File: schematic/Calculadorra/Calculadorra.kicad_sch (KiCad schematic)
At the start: 24 parts, among them U1 ATmega328-P, U2 LCD-016N002L

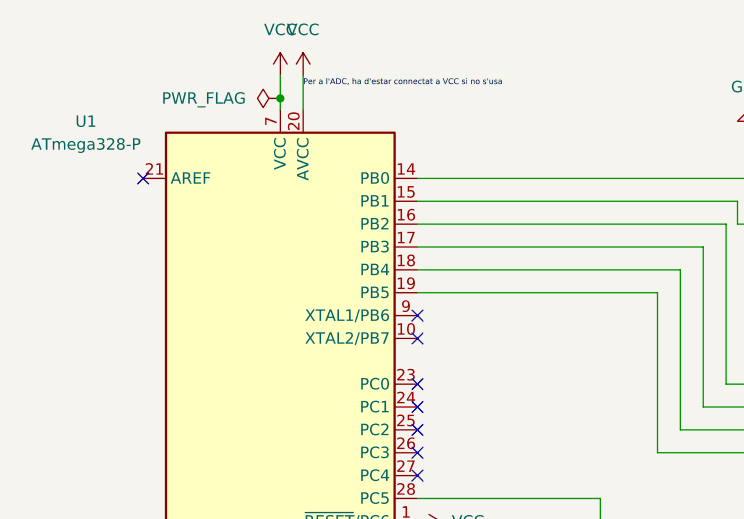
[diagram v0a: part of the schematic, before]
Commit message: Fix scan matrix for 5x4
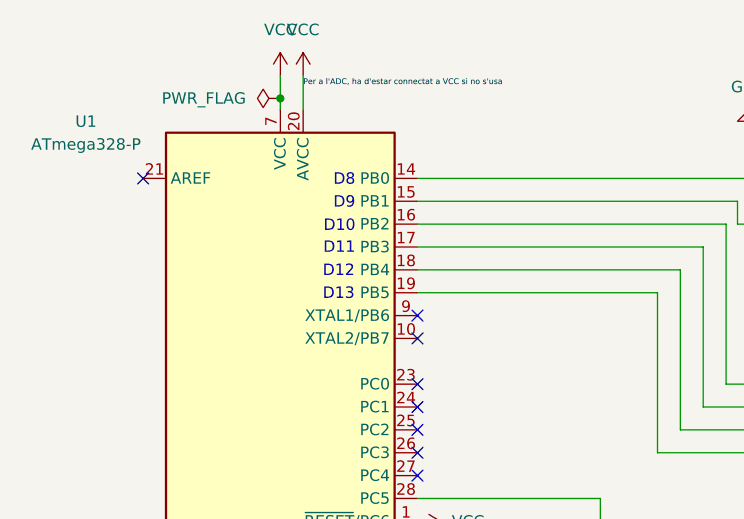
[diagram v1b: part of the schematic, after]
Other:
- note added: "D10"
- note added: "D11"
- note added: "D12"
- note added: "D13"
- note added: "D8"
- note added: "D9"
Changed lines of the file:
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@@
+		)
+	)
+	(text "D11"
+		(exclude_from_sim no)
+		(at 71.3163 58.6163 0)
+		(effects
+			(font
+				(size 1.27 1.27)
+			)
+		)
+	)
+	(text "D13"
+		(exclude_from_sim no)
+		(at 71.2559 63.7354 0)
+		(effects
+			(font
+				(size 1.27 1.27)
+			)
+		)
+	)
+	(text "D9"
+		(exclude_from_sim no)
+		(at 71.882 53.594 0)
+		(effects
+			(font
+				(size 1.27 1.27)
+			)
+		)
+	)
+	(text "D12"
+		(exclude_from_sim no)
+		(at 71.2596 61.1947 0)
+		(effects
+			(font
+				(size 1.27 1.27)
+			)
+		)
+	)
+	(text "D8"
+		(exclude_from_sim no)
+		(at 71.882 51.054 0)
+		(effects
+			(font
+				(size 1.27 1.27)
+			)
+		)
+	)
+	(text "D10"
+		(exclude_from_sim no)
+		(at 71.3446 56.1795 0)
+		(effects
+			(font
+				(size 1.27 1.27)
+			)
 		)
 	)

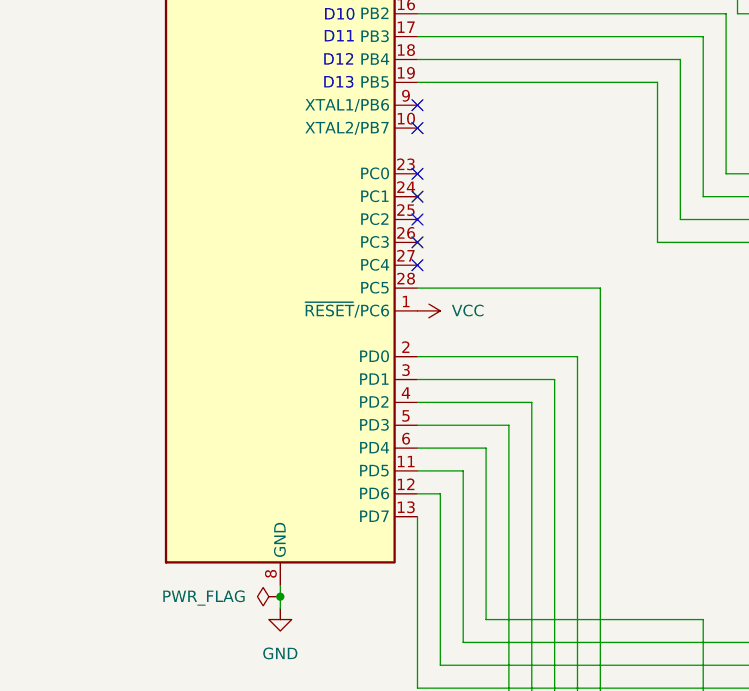
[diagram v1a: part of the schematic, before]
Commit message: Add arduino uno schematics to mega320p
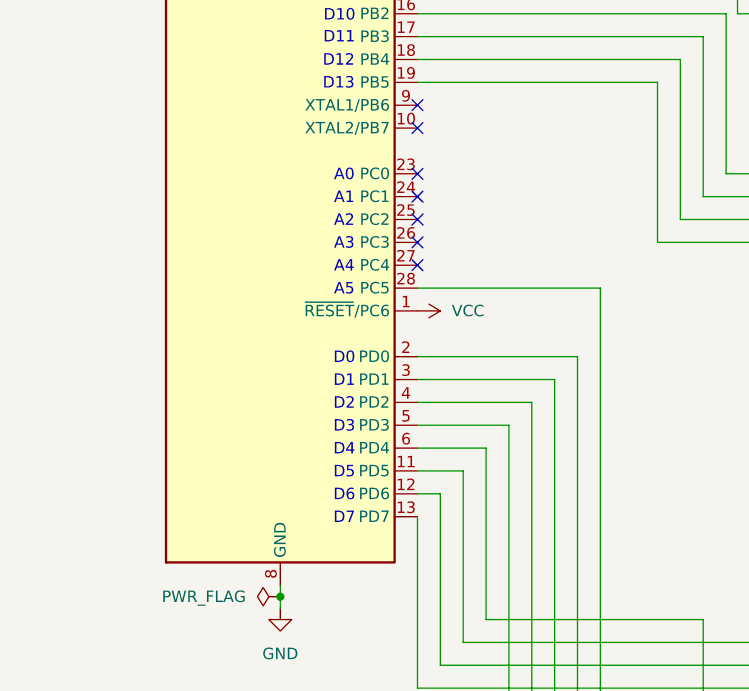
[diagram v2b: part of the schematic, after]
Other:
- note added: "A0"
- note added: "A1"
- note added: "A2"
- note added: "A3"
- note added: "A4"
- note added: "A5"
- note added: "D0"
- note added: "D1"
- note added: "D2"
- note added: "D3"
- note added: "D4"
- note added: "D5"
- note added: "D6"
- note added: "D7"
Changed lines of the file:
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@@
+		)
+	)
+	(text "D4"
+		(exclude_from_sim no)
+		(at 71.882 104.394 0)
+		(effects
+			(font
+				(size 1.27 1.27)
+			)
 		)
 	)
@@
 		)
 	)
+	(text "D3"
+		(exclude_from_sim no)
+		(at 71.882 101.854 0)
+		(effects
+			(font
+				(size 1.27 1.27)
+			)
+		)
+	)
 	(text "D12"
 		(exclude_from_sim no)
 		(at 71.2596 61.1947 0)
+		(effects
+			(font
+				(size 1.27 1.27)
+			)
+		)
+	)
+	(text "D1"
+		(exclude_from_sim no)
+		(at 71.882 96.774 0)
+		(effects
+			(font
+				(size 1.27 1.27)
+			)
+		)
+	)
+	(text "A1"
+		(exclude_from_sim no)
+		(at 71.882 76.454 0)
+		(effects
+			(font
+				(size 1.27 1.27)
+			)
+		)
+	)
+	(text "D0"
+		(exclude_from_sim no)
+		(at 71.882 94.234 0)
+		(effects
+			(font
+				(size 1.27 1.27)
+			)
+		)
+	)
+	(text "D7"
+		(exclude_from_sim no)
+		(at 71.882 112.014 0)
 		(effects
 			(font
@@
 		)
 	)
+	(text "A0\n"
+		(exclude_from_sim no)
+		(at 71.882 73.914 0)
+		(effects
+			(font
+				(size 1.27 1.27)
+			)
+		)
+	)
+	(text "A3"
+		(exclude_from_sim no)
+		(at 71.882 81.534 0)
+		(effects
+			(font
+				(size 1.27 1.27)
+			)
+		)
+	)
+	(text "A4"
+		(exclude_from_sim no)
+		(at 71.882 84.074 0)
+		(effects
+			(font
+				(size 1.27 1.27)
+			)
+		)
+	)
+	(text "D6"
+		(exclude_from_sim no)
+		(at 71.882 109.474 0)
+		(effects
+			(font
+				(size 1.27 1.27)
+			)
+		)
+	)
 	(text "D10"
 		(exclude_from_sim no)
@@
 		(effects
 			(font
+				(size 1.27 1.27)
+			)
+		)
+	)
+	(text "D5"
+		(exclude_from_sim no)
+		(at 71.882 106.934 0)
+		(effects
+			(font
+				(size 1.27 1.27)
+			)
+		)
+	)
+	(text "A5"
+		(exclude_from_sim no)
+		(at 71.882 86.614 0)
+		(effects
+			(font
+				(size 1.27 1.27)
+			)
+		)
+	)
+	(text "D2"
+		(exclude_from_sim no)
+		(at 71.882 99.314 0)
+		(effects
+			(font
+				(size 1.27 1.27)
+			)
+		)
+	)
+	(text "A2"
+		(exclude_from_sim no)
+		(at 71.882 78.994 0)
+		(effects
+			(font

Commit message: No idea what changed
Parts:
- renumbered B_( to B_(1, B_) to B_)1, B_= to B_=1, B_Add to B_Add1, B_Left to B_Left1, B_Mul to B_Mul1, B_On to B_On1, B_Right to B_Right1, B_Shift to B_Shift1, B_Sub to B_Sub1
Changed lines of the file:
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@@
 		(on_board yes)
 		(dnp no)
-		(property "Reference" "B_Left"
+		(property "Reference" "B_Left1"
 			(at 119.38 132.334 0)
 			(effects
@@
 			(project "Calculadorra"
 				(path "/f0879cd9-1f91-4947-9c65-292f7671d223"
-					(reference "B_Left")
+					(reference "B_Left1")
 					(unit 1)
 				)
@@
 		(on_board yes)
 		(dnp no)
-		(property "Reference" "B_Right"
+		(property "Reference" "B_Right1"
 			(at 132.08 132.334 0)
 			(effects
@@
 			(project "Calculadorra"
 				(path "/f0879cd9-1f91-4947-9c65-292f7671d223"
-					(reference "B_Right")
+					(reference "B_Right1")
 					(unit 1)
 				)
@@
 		(dnp no)
 		(fields_autoplaced yes)
-		(property "Reference" "B_="
+		(property "Reference" "B_=1"
 			(at 144.78 172.72 0)
 			(effects
@@
 			(project "Calculadorra"
 				(path "/f0879cd9-1f91-4947-9c65-292f7671d223"
-					(reference "B_=")
+					(reference "B_=1")
 					(unit 1)
 				)
@@
 		(dnp no)
 		(fields_autoplaced yes)
-		(property "Reference" "B_Sub"
+		(property "Reference" "B_Sub1"
 			(at 144.78 152.4 0)
 			(effects
@@
 			(project "Calculadorra"
 				(path "/f0879cd9-1f91-4947-9c65-292f7671d223"
-					(reference "B_Sub")
+					(reference "B_Sub1")
 					(unit 1)
 				)
@@
 		(on_board yes)
 		(dnp no)
-		(property "Reference" "B_Mul"
+		(property "Reference" "B_Mul1"
 			(at 144.78 142.494 0)
 			(effects
@@
 			(project "Calculadorra"
 				(path "/f0879cd9-1f91-4947-9c65-292f7671d223"
-					(reference "B_Mul")
+					(reference "B_Mul1")
 					(unit 1)
 				)
@@
 		(dnp no)
 		(fields_autoplaced yes)
-		(property "Reference" "B_Add"
+		(property "Reference" "B_Add1"
 			(at 144.78 162.56 0)
 			(effects
@@
 			(project "Calculadorra"
 				(path "/f0879cd9-1f91-4947-9c65-292f7671d223"
-					(reference "B_Add")
+					(reference "B_Add1")
 					(unit 1)
 				)
@@
 		(dnp no)
 		(fields_autoplaced yes)
-		(property "Reference" "B_)"
+		(property "Reference" "B_)1"
 			(at 132.08 172.72 0)
 			(effects
@@
 			(project "Calculadorra"
 				(path "/f0879cd9-1f91-4947-9c65-292f7671d223"
-					(reference "B_)")
+					(reference "B_)1")
 					(unit 1)
 				)
@@
 		(on_board yes)
 		(dnp no)
-		(property "Reference" "B_On"
+		(property "Reference" "B_On1"
 			(at 144.78 132.334 0)
 			(effects
@@
 			(project "Calculadorra"
 				(path "/f0879cd9-1f91-4947-9c65-292f7671d223"
-					(reference "B_On")
+					(reference "B_On1")
 					(unit 1)
 				)
@@
 		(on_board yes)
 		(dnp no)
-		(property "Reference" "B_Shift"
+		(property "Reference" "B_Shift1"
 			(at 106.68 132.334 0)
 			(effects
@@
 			(project ""
 				(path "/f0879cd9-1f91-4947-9c65-292f7671d223"
-					(reference "B_Shift")
+					(reference "B_Shift1")
 					(unit 1)
 				)
@@
 		(dnp no)
 		(fields_autoplaced yes)
-		(property "Reference" "B_("
+		(property "Reference" "B_(1"
 			(at 119.38 172.72 0)
 			(effects
@@
 			(project "Calculadorra"
 				(path "/f0879cd9-1f91-4947-9c65-292f7671d223"
-					(reference "B_(")
-					(unit 1)
-				)
+					(reference "B_(1")
+					(unit 1)
+				)

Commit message: Disseny de la PCB i model 3D fet durant la Hacknight
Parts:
- removed U2: LCD-016N002L, Display:LCD-016N002L, symbol Display_Character:LCD-016N002L
- added DS1: WC1602A, Display:WC1602A, symbol Display_Character:WC1602A
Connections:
- net GND: now also DS1.1 (VSS), DS1.16 (LED(-)), DS1.5 (R/W)
- net VCC: now also DS1.2 (VDD)
- net at R1.1: now also DS1.15 (LED(+))
- net at RV1.2: now also DS1.3 (VO)
- net at U1.16 (PB2): now also DS1.11 (D4)
- net at U1.17 (PB3): now also DS1.12 (D5)
- net at U1.18 (PB4): now also DS1.13 (D6)
- net at U1.19 (PB5): now also DS1.14 (D7)
- net at U1.15 (PB1): now also DS1.4 (RS)
- net at U1.14 (PB0): now also DS1.6 (E)
- no-connect marks 16 -> 8

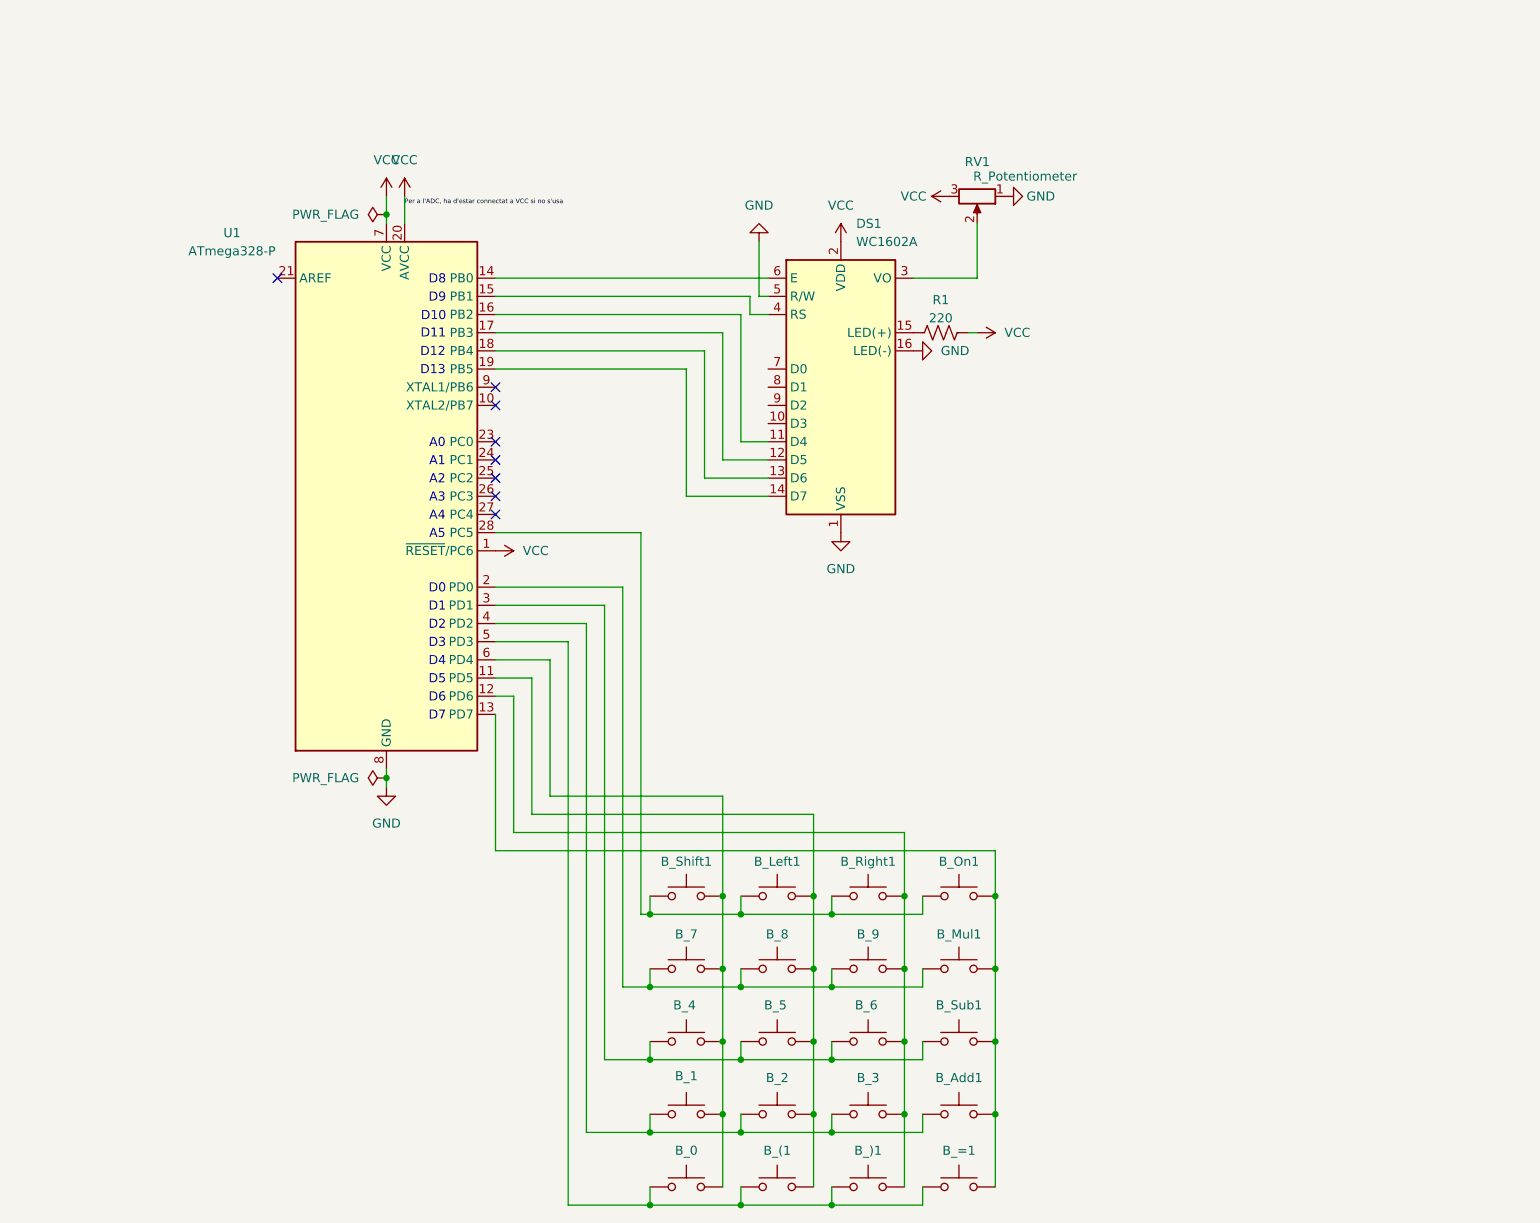
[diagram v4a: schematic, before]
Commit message: PCB amb nous botons, ja posarem díodes i cables en altres moments
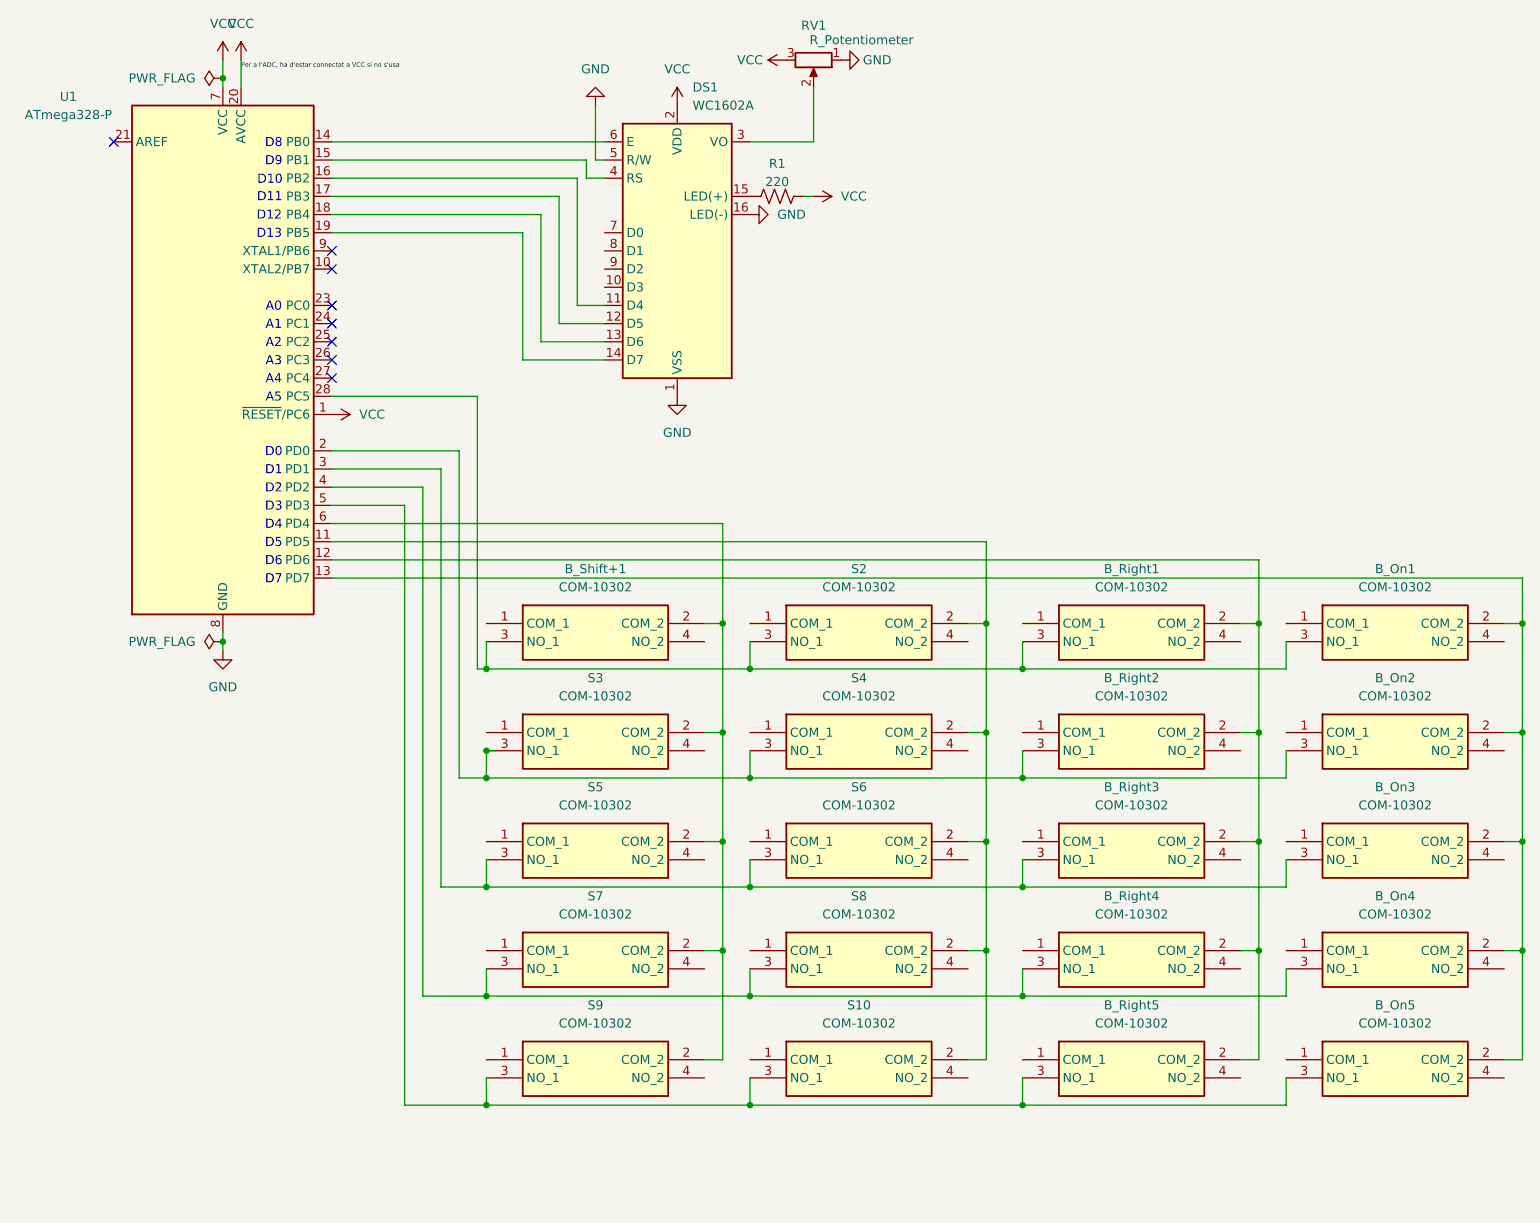
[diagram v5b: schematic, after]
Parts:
- removed B_(1, B_)1, B_0, B_1, B_2, B_3, B_4, B_5, B_6, B_7, B_8, B_9, B_=1, B_Add1, B_Left1, B_Mul1, B_On1, B_Right1, B_Shift1, B_Sub1: SW_Push, Button_Switch_Keyboard:SW_Cherry_MX_1.00u_PCB, symbol Switch:SW_Push
- added B_On1, B_On2, B_On3, B_On4, B_On5, B_Right1, B_Right2, B_Right3, B_Right4, B_Right5, B_Shift+1, S10, S2, S3, S4, S5, S6, S7, S8, S9: COM-10302, Library:Button_COM10302, symbol Button_Gerard:COM-10302
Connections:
- net at U1.3 (PD1): now also B_On3.3 (NO_1), B_Right3.3 (NO_1), S5.3 (NO_1), S6.3 (NO_1)
- net at U1.6 (PD4): now also B_Shift+1.2 (COM_2), S3.2 (COM_2), S5.2 (COM_2), S7.2 (COM_2), S9.2 (COM_2)
- net at U1.28 (PC5): now also B_On1.3 (NO_1), B_Right1.3 (NO_1), B_Shift+1.3 (NO_1), S2.3 (NO_1)
- net at U1.11 (PD5): now also S10.2 (COM_2), S2.2 (COM_2), S4.2 (COM_2), S6.2 (COM_2), S8.2 (COM_2)
- net at U1.2 (PD0): now also B_On2.3 (NO_1), B_Right2.3 (NO_1), S3.3 (NO_1), S4.3 (NO_1)
- net at U1.12 (PD6): now also B_Right1.2 (COM_2), B_Right2.2 (COM_2), B_Right3.2 (COM_2), B_Right4.2 (COM_2), B_Right5.2 (COM_2)
- net at U1.4 (PD2): now also B_On4.3 (NO_1), B_Right4.3 (NO_1), S7.3 (NO_1), S8.3 (NO_1)
- net at U1.5 (PD3): now also B_On5.3 (NO_1), B_Right5.3 (NO_1), S10.3 (NO_1), S9.3 (NO_1)
- net at U1.13 (PD7): now also B_On1.2 (COM_2), B_On2.2 (COM_2), B_On3.2 (COM_2), B_On4.2 (COM_2), B_On5.2 (COM_2)
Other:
- moved on the sheet: DS1, R1, RV1, U1
